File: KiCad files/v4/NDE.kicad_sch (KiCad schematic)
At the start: 17 parts, among them J1 Nabíjací modul, J14 VM_Select, J2 Step-up input, J3 Step-up output, U1 LM7805_TO220

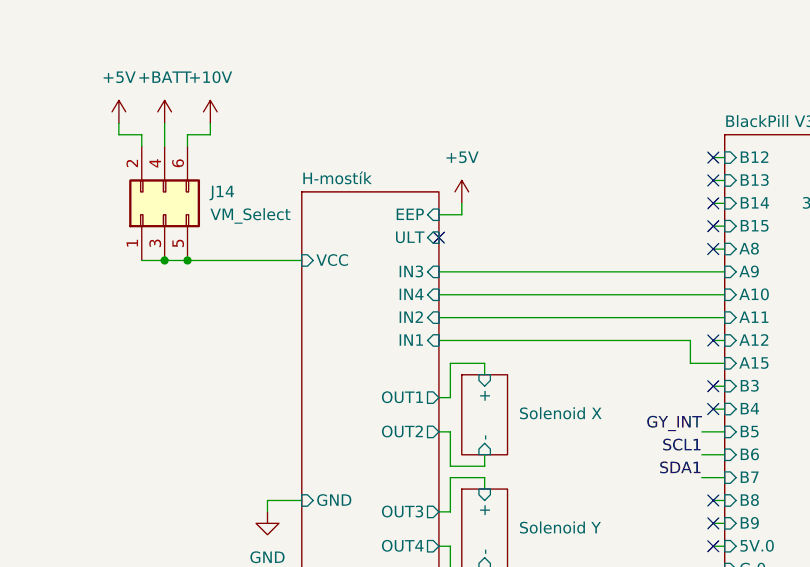
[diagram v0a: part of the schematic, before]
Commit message: Fixed unconnected GND of MCU and flipped H-bridge sockets
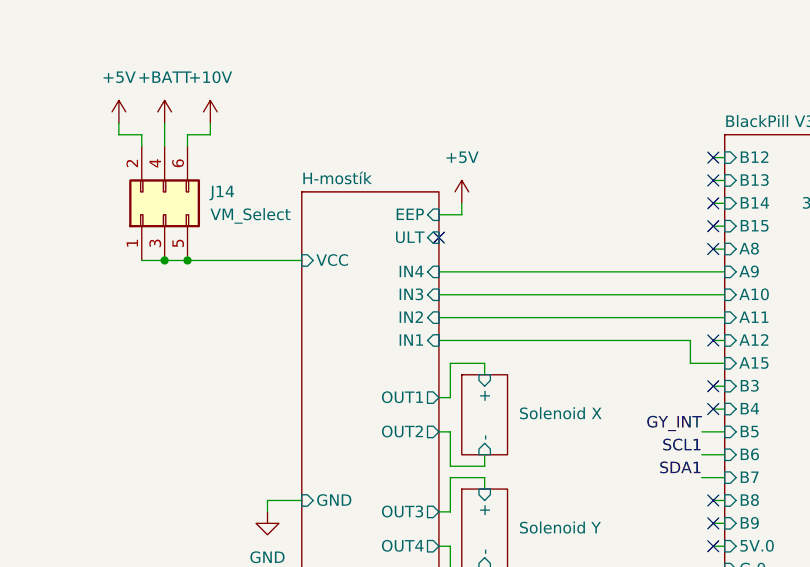
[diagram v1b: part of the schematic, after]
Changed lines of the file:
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@@
 	(wire
 		(pts
-			(xy 130.81 90.17) (xy 162.56 90.17)
-		)
-		(stroke
-			(width 0)
-			(type default)
-		)
-	)
-	(wire
-		(pts
 			(xy 132.08 116.84) (xy 132.08 113.03)
 		)
@@
 	(wire
 		(pts
+			(xy 130.81 92.71) (xy 162.56 92.71)
+		)
+		(stroke
+			(width 0)
+			(type default)
+		)
+	)
+	(wire
+		(pts
 			(xy 161.29 85.09) (xy 162.56 85.09)
 		)
@@
 	(wire
 		(pts
+			(xy 130.81 90.17) (xy 162.56 90.17)
+		)
+		(stroke
+			(width 0)
+			(type default)
+		)
+	)
+	(wire
+		(pts
 			(xy 62.23 64.77) (xy 62.23 63.5)
 		)
@@
 	(wire
 		(pts
-			(xy 130.81 92.71) (xy 162.56 92.71)
-		)
-		(stroke
-			(width 0)
-			(type default)
-		)
-	)
-	(wire
-		(pts
 			(xy 234.95 133.35) (xy 233.68 133.35)
 		)
@@
 		)
 		(pin "IN3" input
-			(at 130.81 90.17 0)
+			(at 130.81 92.71 0)
 			(effects
 				(font
@@
 		)
 		(pin "IN4" input
-			(at 130.81 92.71 0)
+			(at 130.81 90.17 0)
 			(effects
 				(font

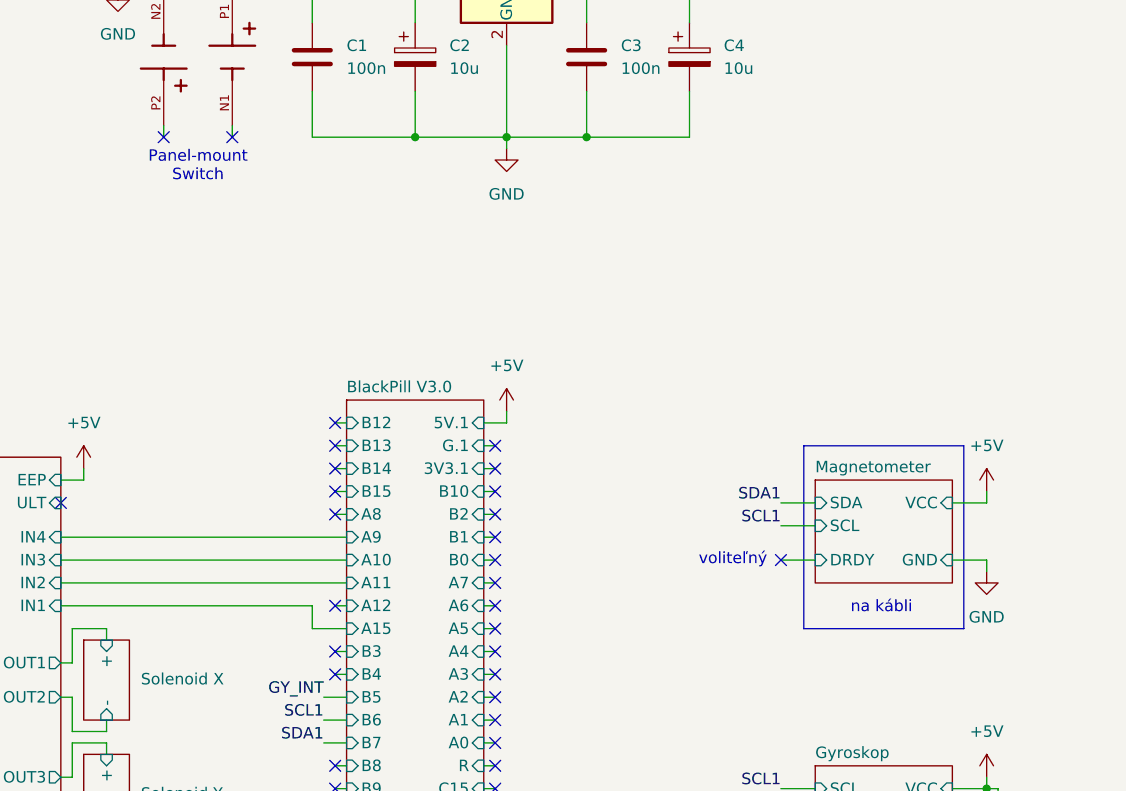
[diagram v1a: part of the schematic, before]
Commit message: Generated output files for docs. Removed old fabrication files.
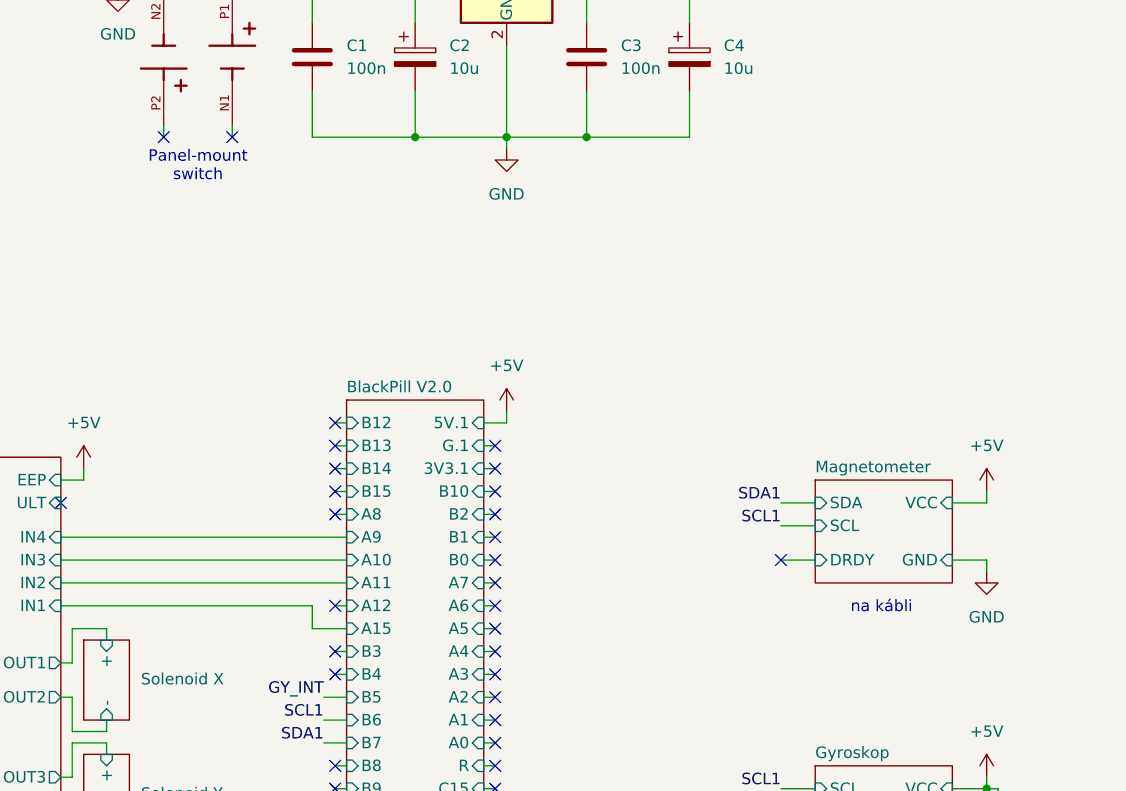
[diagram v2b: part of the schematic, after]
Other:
- sheet BlackPill V3.0 renamed BlackPill V2.0
- note added: "Panel-mount switch"
- note removed: "Panel-mount Switch"
- note removed: "voliteľný"
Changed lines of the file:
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@@
 		)
 	)
-	(rectangle
-		(start 231.14 80.01)
-		(end 213.36 100.33)
-		(stroke
-			(width 0)
-			(type default)
-		)
-		(fill
-			(type none)
-		)
-	)
-	(text "voliteľný"
-		(exclude_from_sim no)
-		(at 205.486 92.71 0)
-		(effects
-			(font
-				(size 1.27 1.27)
-			)
-		)
-	)
 	(text "Prídavné konektory \nna externý DC/DC menič"
 		(exclude_from_sim no)
@@
 		)
 	)
-	(text "Panel-mount\nSwitch"
+	(text "Panel-mount\nswitch"
 		(exclude_from_sim no)
 		(at 146.05 49.022 0)
@@
 			(color 0 0 0 0.0000)
 		)
-		(property "Sheetname" "BlackPill V3.0"
+		(property "Sheetname" "BlackPill V2.0"
 			(at 162.56 74.2184 0)
 			(effects
